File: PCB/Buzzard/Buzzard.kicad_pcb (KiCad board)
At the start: 2 copper layers, 150.2 x 93.9 mm, 87 parts, among them J2 LCD, J4 Haptic Buzz, J5 TrackPoint, J6 OLED, J8 Battery, SW1 SW_DPST_x2, U1 ProMicro, U10 Hole, U11 Hole, U12 Hole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

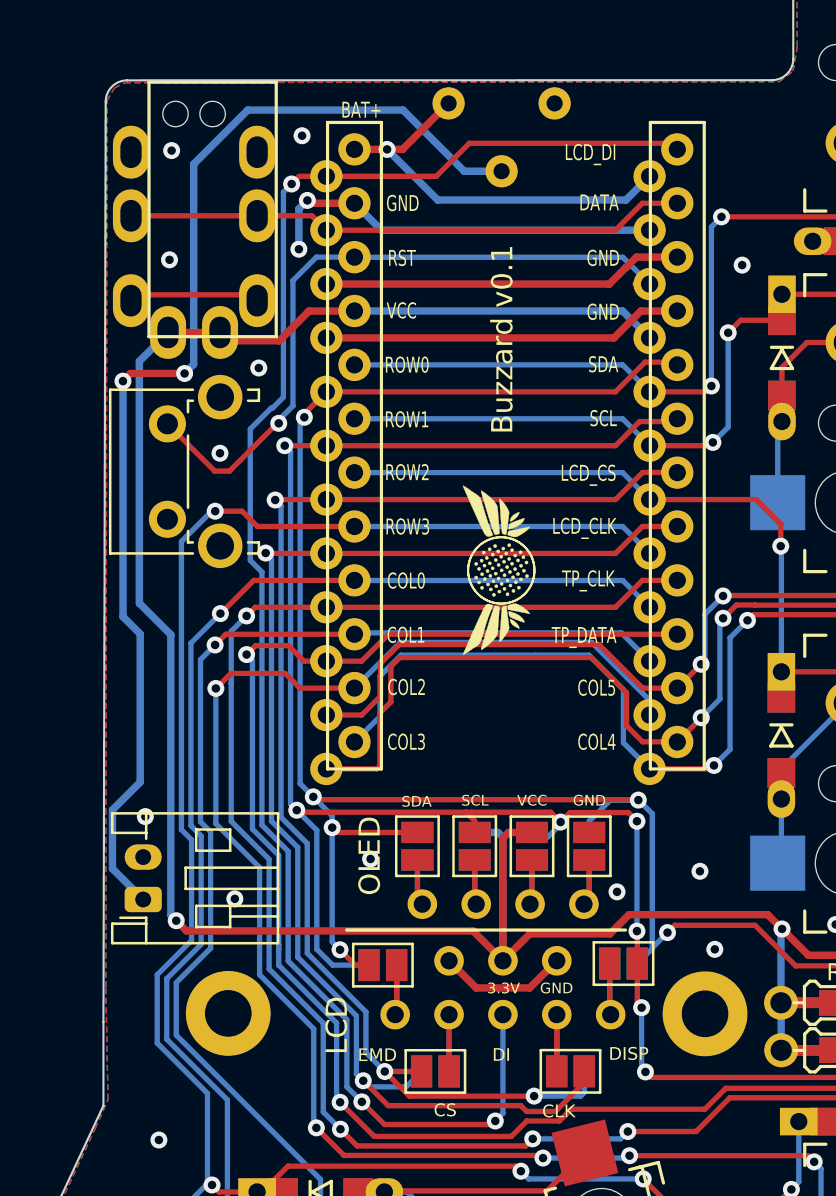
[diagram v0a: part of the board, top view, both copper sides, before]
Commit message: switched trrs lines and TP clock/data lines
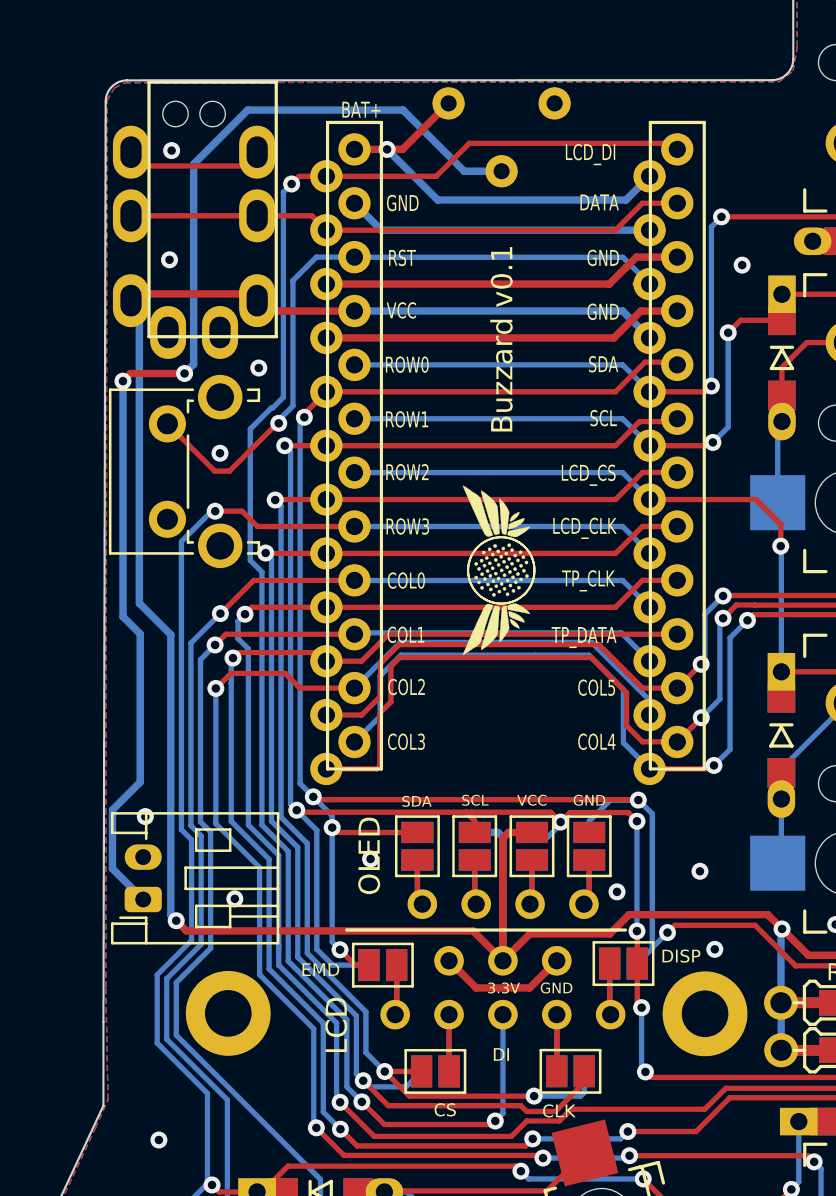
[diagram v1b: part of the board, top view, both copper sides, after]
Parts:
- renumbered Je to J1, Reset to SW2
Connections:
- J1 pad 1: unconnected-(J1-Pad1) -> VCC
- J1 pad 3: GND -> unconnected-(J1-Pad3)
- J1 pad 4: VCC -> GND
- U1 pad 10: TP_DATA -> TP_CLK
- U1 pad 9: TP_CLK -> TP_DATA
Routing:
- net unconnected-(J1-Pad3): track 0.00 -> 6.49 mm
- net unconnected-(J1-Pad1): track 6.18 -> 0.00 mm
- net GND: track 59.6 -> 54.9 mm, vias 32 -> 29
- net VCC: track 188.9 -> 191.9 mm
- net TP_DATA: track 128.0 -> 130.0 mm
- net TP_CLK: track 132.7 -> 131.2 mm

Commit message: Some fine tuning and silkmask improvments
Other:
- board size 150.2 x 93.9 mm -> 150 x 93.8 mm
- board text added: "Bat+"
- board text added: "Bat-"
- board text added: "Buzzard Rev1"
- board text removed: "Buzzard v0.1"
